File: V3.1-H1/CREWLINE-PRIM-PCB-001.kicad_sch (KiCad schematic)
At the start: 74 parts, among them J1 BATTERY, J2 CHARGE SHIELD HEADER, J3 DIO, J4 PWR INPUTS, J5 CAN CABLES, J6 SEAT_CONNECTOR, J7 BRAKE INPUTS, J8 SAFETY_CONNECTOR, J9 Conn_02x06_Counter_Clockwise, Q1 IRF4905STRL

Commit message: Add brake and E-stop relay logic to the schematic
Extend J7 to 7 positions and add J10 for the E-stop lines. Add the
child sheet brake-estop.kicad_sch with K_BRAKE_CAT1/2, K_ESTOP_BOMAG1/2
and K_ESTOP_CAT1/2, and move K_BRAKE_BOMAG1 onto it. Each coil that a
Jetson output feeds has a series 1N4148WS diode.

Add five signal test points. Clear the six stale DNP flags. Replace the
3 mm LED symbols with the generic LED symbol so pin 1 is the cathode,
which matches the 0805 footprint. Recover the custom symbol and
footprint libraries into lib/ and register them in the project tables.
Add a 7-way MCV 1.5 footprint with 2.6 mm pads.

Co-Authored-By: Claude Fable 5.1 <noreply@anthropic.com>
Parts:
- removed BRK-Relay-LED1: Green, LED_SMD:LED_0805_2012Metric, symbol Device:LED
- removed BRK-Relay-RES1: 2.2k, Resistor_SMD:R_0805_2012Metric, symbol Device:R
- removed D_KBRAKE1: D, 1N4148WS:SOD-323_L1.8-W1.3-LS2.5-RD, symbol Device:D
- removed K_BRAKE1: Relay_DPDT, Relay_THT:Relay_DPDT_Omron_G6A, symbol Relay:Relay_DPDT
- added BRK_ECU_NF_TP1, BRK_ECU_NG_TP1, ESTP_ECU_NF_TP1, ESTP_ECU_NG_TP1, ESTP_ECU_TP1: TestPoint, TestPoint_Black:TEST-TH_BD2.54-P1.4_BLACK, symbol Connector:TestPoint
- added J10: ESTOP INPUTS, V31_H1:MCV_1.5_7_5.08_Pad2.6, symbol Connector:Conn_01x07_Socket
- C1, J1, J9, K_ECUCAN1, K_JOYCAN1: now fitted
- CONV_LED1, DIO_LED1, JET_LED1, LED_LED1, PWR_LIGHT1, STR_LED1: symbol LED_3mm_Red:204-10SDRD_S530-A3-L -> Device:LED; LCSC Part C84256 -> (none); MPN 204-10SDRD/S530-A3-L -> (none); Manufacturer EVERLIGHT(亿光) -> (none)
- J7: footprint V31_H1:MCV_1.5_4_5.08_Pad2.6 -> V31_H1:MCV_1.5_7_5.08_Pad2.6; symbol Connector:Conn_01x04_Socket -> Connector:Conn_01x07_Socket; MPN 1836312 -> 1836341; Mating plug 1836095 -> 1836121
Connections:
- net +12V_KIT: now also PWR_LIGHT1.2 (A); no longer PWR_LIGHT1.1 (A)
- net CONV_PWR_P: now also CONV_LED1.2 (A); no longer CONV_LED1.1 (A)
- net JETSON_PWR_P: now also JET_LED1.2 (A); no longer JET_LED1.1 (A)
- net JET_DIO_PWR_P: now also DIO_LED1.2 (A); no longer DIO_LED1.1 (A)
- net LED_PWR_P: now also LED_LED1.2 (A); no longer LED_LED1.1 (A)
- net STEER_PWR_P: now also STR_LED1.2 (A); no longer STR_LED1.1 (A)
- net at DIO_RES1.1: now also DIO_LED1.1 (K); no longer DIO_LED1.2 (C)
- net at STR_RES1.1: now also STR_LED1.1 (K); no longer STR_LED1.2 (C)
- net at D2.2 (A), R_ARMED1.1: now also PWR_LIGHT1.1 (K); no longer PWR_LIGHT1.2 (C)
- net at LED_RES1.1: now also LED_LED1.1 (K); no longer LED_LED1.2 (C)
- net at CONV_RES1.1: now also CONV_LED1.1 (K); no longer CONV_LED1.2 (C)
- net at JET_RES1.1: now also JET_LED1.1 (K); no longer JET_LED1.2 (C)
- net BRAKE_JOY_NG: now reaches J7.4 (Pin_4)
- new net BRAKE_ECU_NF: BRK_ECU_NF_TP1.1, J7.7 (Pin_7)
- new net BRAKE_ECU_NG: BRK_ECU_NG_TP1.1, J7.6 (Pin_6)
- new net BRAKE_JOY_NF: J7.5 (Pin_5)
- new net ESTOP_ECU: ESTP_ECU_TP1.1, J10.3 (Pin_3)
- new net ESTOP_ECU_NF: ESTP_ECU_NF_TP1.1, J10.7 (Pin_7)
- new net ESTOP_ECU_NG: ESTP_ECU_NG_TP1.1, J10.6 (Pin_6)
- new net ESTOP_JET: J10.1 (Pin_1)
- new net ESTOP_JOY: J10.2 (Pin_2)
- new net ESTOP_JOY_NF: J10.5 (Pin_5)
- new net ESTOP_JOY_NG: J10.4 (Pin_4)
- no-connect marks 12 -> 8
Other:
- added sheet Brake and E-stop (brake-estop.kicad_sch)
- note added: "ESTOP CONNECTOR"
- note removed: "BRAKE RELAY"

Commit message: Keep the red LED polarity as built
The boards in service light with the anode on pad 1, so the LED symbol
keeps pin 1 as the anode. The symbol moves to the project library as
LED_Red_0805_A1 with the polarity written in its description, and the
3 mm part number fields are removed.

Co-Authored-By: Claude Fable 5.1 <noreply@anthropic.com>
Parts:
- CONV_LED1, DIO_LED1, JET_LED1, LED_LED1, PWR_LIGHT1, STR_LED1: symbol Device:LED -> V31_H1:LED_Red_0805_A1
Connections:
- net +12V_KIT: now also PWR_LIGHT1.1 (A); no longer PWR_LIGHT1.2 (A)
- net CONV_PWR_P: now also CONV_LED1.1 (A); no longer CONV_LED1.2 (A)
- net JETSON_PWR_P: now also JET_LED1.1 (A); no longer JET_LED1.2 (A)
- net JET_DIO_PWR_P: now also DIO_LED1.1 (A); no longer DIO_LED1.2 (A)
- net LED_PWR_P: now also LED_LED1.1 (A); no longer LED_LED1.2 (A)
- net STEER_PWR_P: now also STR_LED1.1 (A); no longer STR_LED1.2 (A)
- net at DIO_RES1.1: now also DIO_LED1.2 (C); no longer DIO_LED1.1 (K)
- net at STR_RES1.1: now also STR_LED1.2 (C); no longer STR_LED1.1 (K)
- net at D2.2 (A), R_ARMED1.1: now also PWR_LIGHT1.2 (C); no longer PWR_LIGHT1.1 (K)
- net at LED_RES1.1: now also LED_LED1.2 (C); no longer LED_LED1.1 (K)
- net at CONV_RES1.1: now also CONV_LED1.2 (C); no longer CONV_LED1.1 (K)
- net at JET_RES1.1: now also JET_LED1.2 (C); no longer JET_LED1.1 (K)
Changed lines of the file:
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@@
 	)
 	(symbol
-		(lib_id "Device:LED")
-		(at 227.33 133.35 180)
+		(lib_id "V31_H1:LED_Red_0805_A1")
+		(at 228.6 132.08 0)
 		(unit 1)
 		(body_style 1)
@@
 			)
 		)
-		(property "Description" "Red LED, 0805"
+		(property "Description" "Red LED, 0805. Pin 1 is the anode, which matches the boards as built."
 			(at 228.6 132.08 0)
 			(hide yes)
@@
 	)
 	(symbol
-		(lib_id "Device:LED")
-		(at 111.76 190.5 180)
+		(lib_id "V31_H1:LED_Red_0805_A1")
+		(at 113.03 189.23 0)
 		(unit 1)
 		(body_style 1)
@@
 			)
 		)
-		(property "Description" "Red LED, 0805"
+		(property "Description" "Red LED, 0805. Pin 1 is the anode, which matches the boards as built."
 			(at 113.03 189.23 0)
 			(hide yes)
@@
 	)
 	(symbol
-		(lib_id "Device:LED")
-		(at 196.85 129.54 0)
+		(lib_id "V31_H1:LED_Red_0805_A1")
+		(at 195.58 130.81 180)
 		(unit 1)
 		(body_style 1)
@@
 			)
 		)
-		(property "Description" "Red LED, 0805"
+		(property "Description" "Red LED, 0805. Pin 1 is the anode, which matches the boards as built."
 			(at 195.58 130.81 0)
 			(hide yes)
@@
 	)
 	(symbol
-		(lib_id "Device:LED")
-		(at 193.04 29.21 90)
+		(lib_id "V31_H1:LED_Red_0805_A1")
+		(at 194.31 30.48 270)
 		(unit 1)
 		(body_style 1)
@@
 			)
 		)
-		(property "Description" "Red LED, 0805"
+		(property "Description" "Red LED, 0805. Pin 1 is the anode, which matches the boards as built."
 			(at 194.31 30.48 0)
 			(hide yes)
@@
 	)
 	(symbol
-		(lib_id "Device:LED")
-		(at 227.33 147.32 180)
+		(lib_id "V31_H1:LED_Red_0805_A1")
+		(at 228.6 146.05 0)
 		(unit 1)
 		(body_style 1)
@@
 			)
 		)
-		(property "Description" "Red LED, 0805"
+		(property "Description" "Red LED, 0805. Pin 1 is the anode, which matches the boards as built."
 			(at 228.6 146.05 0)
 			(hide yes)
@@
 	)
 	(symbol
-		(lib_id "Device:LED")
-		(at 196.85 142.24 0)
+		(lib_id "V31_H1:LED_Red_0805_A1")
+		(at 195.58 143.51 180)
 		(unit 1)
 		(body_style 1)
@@
 			)
 		)
-		(property "Description" "Red LED, 0805"
+		(property "Description" "Red LED, 0805. Pin 1 is the anode, which matches the boards as built."
 			(at 195.58 143.51 0)
 			(hide yes)
@@
 	)
 	(embedded_fonts no)
-	(wire
-		(pts
-			(xy 231.14 133.35) (xy 233.68 133.35)
-		)
-		(stroke
-			(width 0)
-			(type default)
-		)
-	)
-	(wire
-		(pts
-			(xy 115.57 190.5) (xy 118.11 190.5)
-		)
-		(stroke
-			(width 0)
-			(type default)
-		)
-	)
-	(wire
-		(pts
-			(xy 193.04 129.54) (xy 190.5 129.54)
-		)
-		(stroke
-			(width 0)
-			(type default)
-		)
-	)
-	(wire
-		(pts
-			(xy 193.04 33.02) (xy 193.04 35.56)
-		)
-		(stroke
-			(width 0)
-			(type default)
-		)
-	)
-	(wire
-		(pts
-			(xy 231.14 147.32) (xy 233.68 147.32)
-		)
-		(stroke
-			(width 0)
-			(type default)
-		)
-	)
-	(wire
-		(pts
-			(xy 193.04 142.24) (xy 190.5 142.24)
-		)
-		(stroke
-			(width 0)
-			(type default)
-		)
-	)
 )

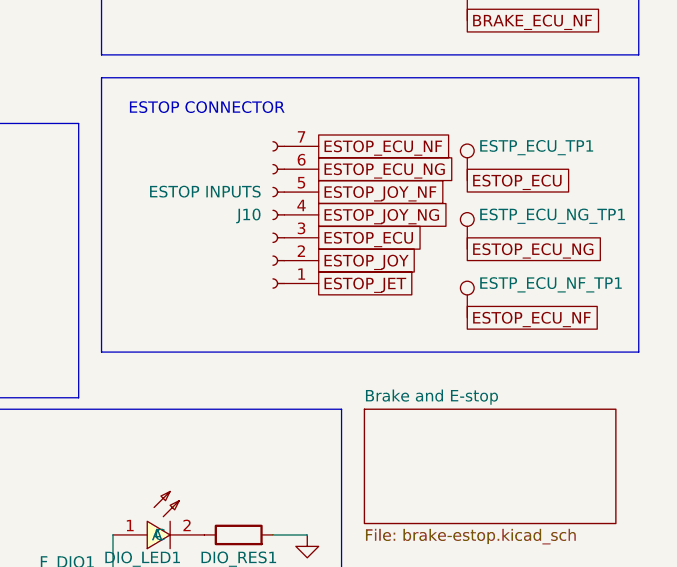
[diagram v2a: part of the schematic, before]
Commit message: Merge the E-stop relays and rename ESTOP_JET to ESTOP_REMOTE
The four E-stop relays become ESTOP_COM_RELAY1 and ESTOP_COM_RELAY2.
Each keeps the coil of its BOMAG relay and takes the CAT contacts on
its spare pole. The support parts follow the new names and the second
series diode is removed.

Co-Authored-By: Claude Fable 5.1 <noreply@anthropic.com>
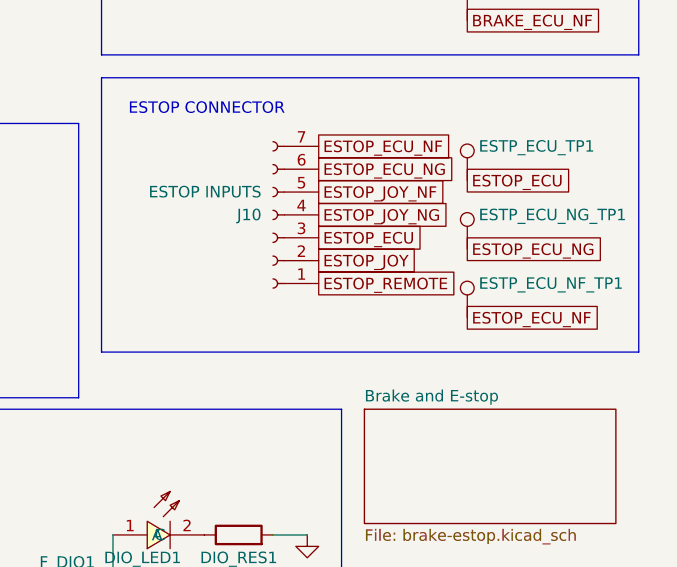
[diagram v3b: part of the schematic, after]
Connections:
- net ESTOP_JET renamed ESTOP_REMOTE
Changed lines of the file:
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@@
 		)
 	)
-	(global_label "ESTOP_JET"
+	(global_label "ESTOP_REMOTE"
 		(shape passive)
 		(at 246.38 105.41 0)
